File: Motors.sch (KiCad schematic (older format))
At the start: 0 parts

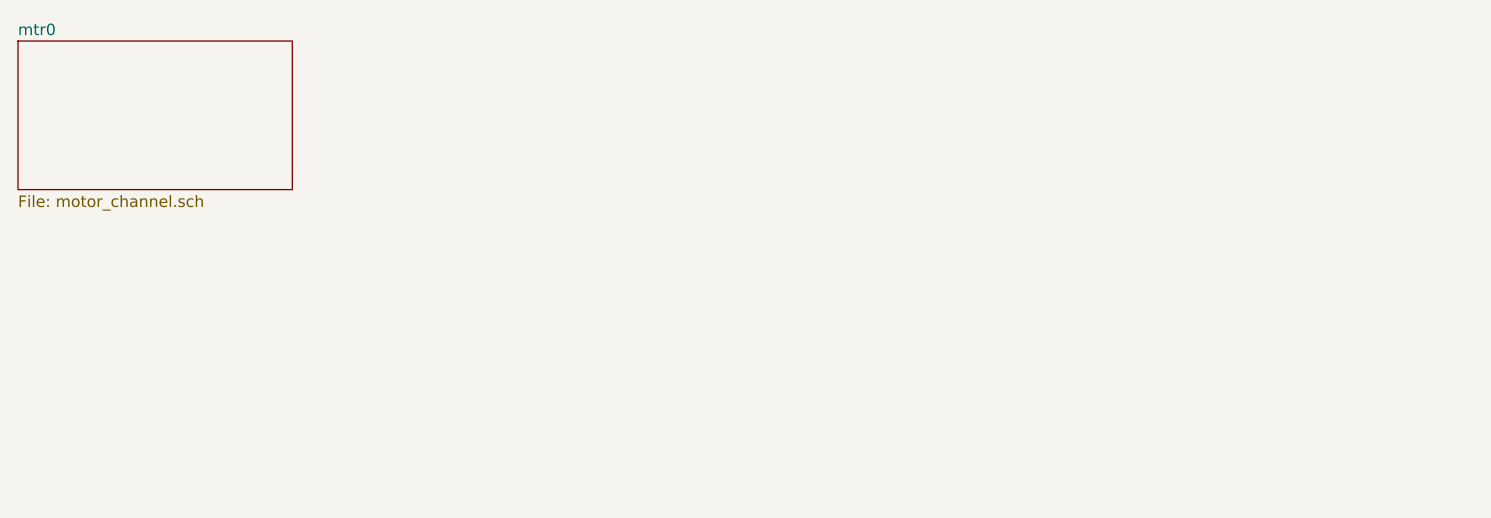
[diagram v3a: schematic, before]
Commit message: Motor channels mostly finished
Todo: Need to determine capacitance of decoupling caps in motor channel.
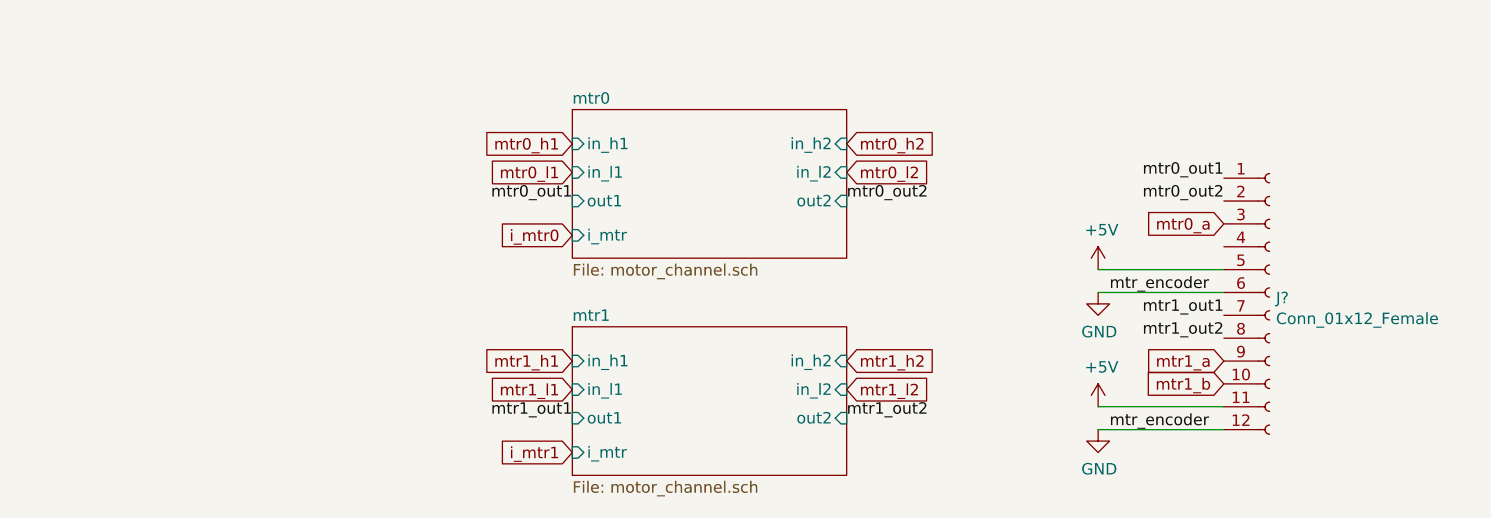
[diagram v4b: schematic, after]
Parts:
- added J?: Conn_01x12_Female, symbol Connector:Conn_01x12_Female
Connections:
- new net +5V: J?.11 (Pin_11), J?.5 (Pin_5)
- new net GND: J?.12 (Pin_12), J?.6 (Pin_6)
- new net mtr0_a: J?.3 (Pin_3)
- new net mtr0_out1: J?.1 (Pin_1)
- new net mtr0_out2: J?.2 (Pin_2)
- new net mtr1_a: J?.9 (Pin_9)
- new net mtr1_b: J?.10 (Pin_10)
- new net mtr1_out1: J?.7 (Pin_7)
- new net mtr1_out2: J?.8 (Pin_8)
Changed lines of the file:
@@
 $Descr A4 11693 8268
 encoding utf-8
-Sheet 10 11
+Sheet 9 12
 Title ""
 Date ""
@@
 $EndDescr
 $Sheet
-S 1100 1050 1200 650
+S 3525 1350 1200 650
 U 5E507A5C
 F0 "mtr0" 50
 F1 "motor_channel.sch" 50
+F2 "in_h1" I L 3525 1500 50
+F3 "in_h2" I R 4725 1500 50
+F4 "in_l1" I L 3525 1625 50
+F5 "in_l2" I R 4725 1625 50
+F6 "i_mtr" I L 3525 1900 50
+F7 "out1" I L 3525 1750 50
+F8 "out2" I R 4725 1750 50
 $EndSheet
+Text Label 3525 1750 2    50   ~ 0
+mtr0_out1
+Text Label 4725 1750 0    50   ~ 0
+mtr0_out2
+Text GLabel 3525 1500 0    50   Input ~ 0
+mtr0_h1
+Text GLabel 3525 1625 0    50   Input ~ 0
+mtr0_l1
+Text GLabel 4725 1500 2    50   Input ~ 0
+mtr0_h2
+Text GLabel 4725 1625 2    50   Input ~ 0
+mtr0_l2
+Text GLabel 3525 1900 0    50   Input ~ 0
+i_mtr0
+$Sheet
+S 3525 2300 1200 650
+U 5E6AD26A
+F0 "mtr1" 50
+F1 "motor_channel.sch" 50
+F2 "in_h1" I L 3525 2450 50
+F3 "in_h2" I R 4725 2450 50
+F4 "in_l1" I L 3525 2575 50
+F5 "in_l2" I R 4725 2575 50
+F6 "i_mtr" I L 3525 2850 50
+F7 "out1" I L 3525 2700 50
+F8 "out2" I R 4725 2700 50
+$EndSheet
+Text Label 3525 2700 2    50   ~ 0
+mtr1_out1
+Text Label 4725 2700 0    50   ~ 0
+mtr1_out2
+Text GLabel 3525 2450 0    50   Input ~ 0
+mtr1_h1
+Text GLabel 3525 2575 0    50   Input ~ 0
+mtr1_l1
+Text GLabel 4725 2450 2    50   Input ~ 0
+mtr1_h2
+Text GLabel 4725 2575 2    50   Input ~ 0
+mtr1_l2
+Text GLabel 3525 2850 0    50   Input ~ 0
+i_mtr1
+$Comp
+L Connector:Conn_01x12_Female J?
+U 1 1 5E6AD3E3
+P 6575 2150
+F 0 "J?" H 6603 2126 50  0000 L CNN
+F 1 "Conn_01x12_Female" H 6603 2035 50  0000 L CNN
+F 2 "" H 6575 2150 50  0001 C CNN
+F 3 "~" H 6575 2150 50  0001 C CNN
+	1    6575 2150
+	1    0    0    -1
+$EndComp
+Text Label 6375 1650 2    50   ~ 0
+mtr0_out1
+Text Label 6375 1750 2    50   ~ 0
+mtr0_out2
+Text GLabel 6375 1850 0    50   Input ~ 0
+mtr0_a
+Text Label 6375 2250 2    50   ~ 0
+mtr1_out1
+Text Label 6375 2350 2    50   ~ 0
+mtr1_out2
+Text GLabel 6375 2450 0    50   Input ~ 0
+mtr1_a
+Text GLabel 6375 2550 0    50   Input ~ 0
+mtr1_b
+Wire Wire Line
+	5825 2050 6375 2050
+Wire Wire Line
+	5825 2150 6375 2150
+Wire Wire Line
+	5825 2650 6375 2650
+Wire Wire Line
+	5825 2750 6375 2750
+$Comp
+L power:+5V #PWR?
+U 1 1 5E6B0E85
+P 5825 2050
+F 0 "#PWR?" H 5825 1900 50  0001 C CNN
+F 1 "+5V" H 5840 2223 50  0000 C CNN
+F 2 "" H 5825 2050 50  0001 C CNN
+F 3 "" H 5825 2050 50  0001 C CNN
+	1    5825 2050
+	1    0    0    -1
+$EndComp
+$Comp
+L power:+5V #PWR?
+U 1 1 5E6B1311
+P 5825 2650
+F 0 "#PWR?" H 5825 2500 50  0001 C CNN
+F 1 "+5V" H 5840 2823 50  0000 C CNN
+F 2 "" H 5825 2650 50  0001 C CNN
+F 3 "" H 5825 2650 50  0001 C CNN
+	1    5825 2650
+	1    0    0    -1
+$EndComp
+$Comp
+L power:GND #PWR?
+U 1 1 5E6B1444
+P 5825 2150
+F 0 "#PWR?" H 5825 1900 50  0001 C CNN
+F 1 "GND" H 5830 1977 50  0000 C CNN
+F 2 "" H 5825 2150 50  0001 C CNN
+F 3 "" H 5825 2150 50  0001 C CNN
+	1    5825 2150
+	1    0    0    -1
+$EndComp
+$Comp
+L power:GND #PWR?
+U 1 1 5E6B180E
+P 5825 2750
+F 0 "#PWR?" H 5825 2500 50  0001 C CNN
+F 1 "GND" H 5830 2577 50  0000 C CNN
+F 2 "" H 5825 2750 50  0001 C CNN
+F 3 "" H 5825 2750 50  0001 C CNN
+	1    5825 2750
+	1    0    0    -1
+$EndComp
+Text Label 5875 2750 0    50   ~ 0
+mtr_encoder
+Text Label 5875 2150 0    50   ~ 0
+mtr_encoder
 $EndSCHEMATC

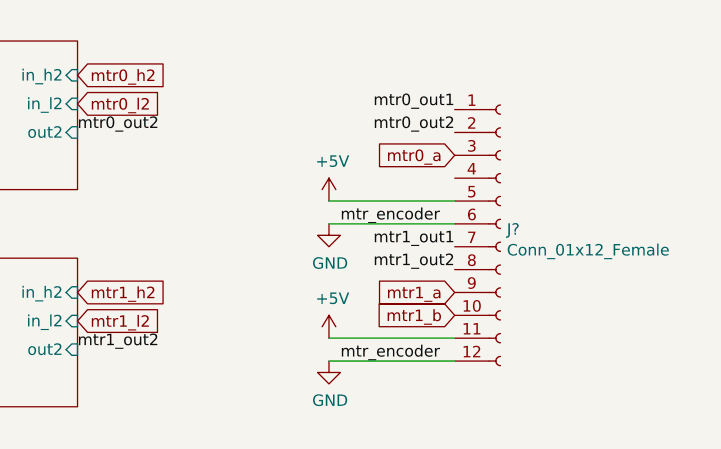
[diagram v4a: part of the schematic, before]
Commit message: hotfix
fixed some labels
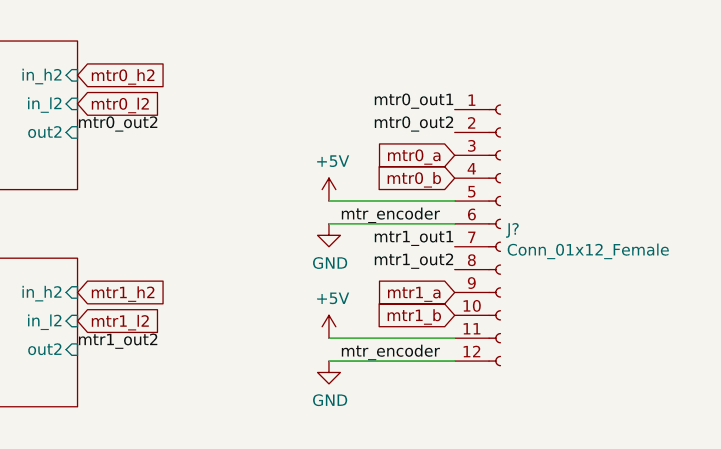
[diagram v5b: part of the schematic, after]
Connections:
- net mtr0_b: now reaches J?.4 (Pin_4)
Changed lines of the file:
@@
 $Descr A4 11693 8268
 encoding utf-8
-Sheet 9 12
+Sheet 10 12
 Title ""
 Date ""
@@
 Text Label 5875 2150 0    50   ~ 0
 mtr_encoder
+Text GLabel 6375 1950 0    50   Input ~ 0
+mtr0_b
 $EndSCHEMATC

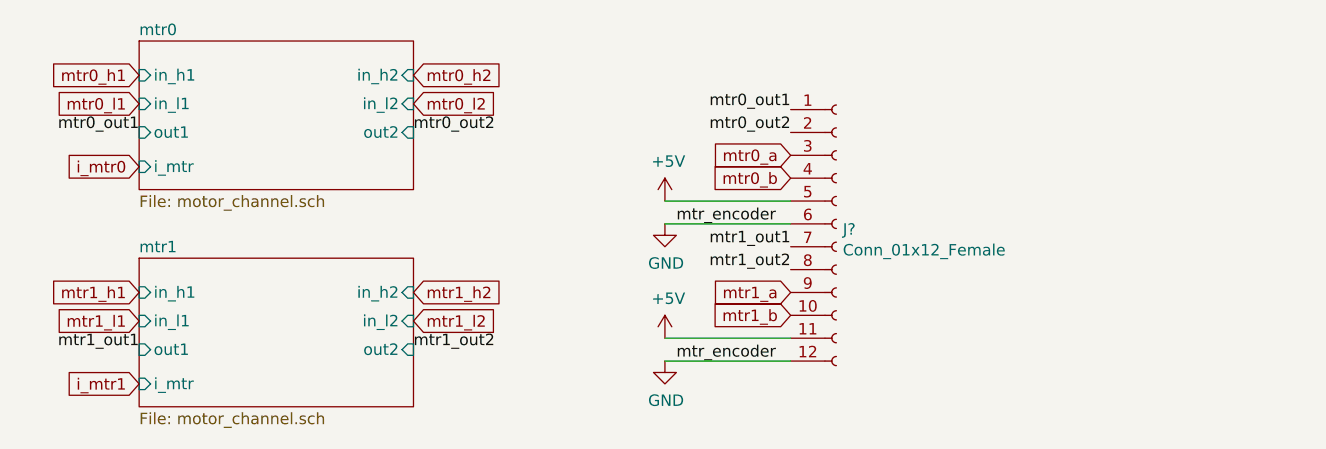
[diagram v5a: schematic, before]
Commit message: Updated Motor Channels
Each motor only needs two inputs.
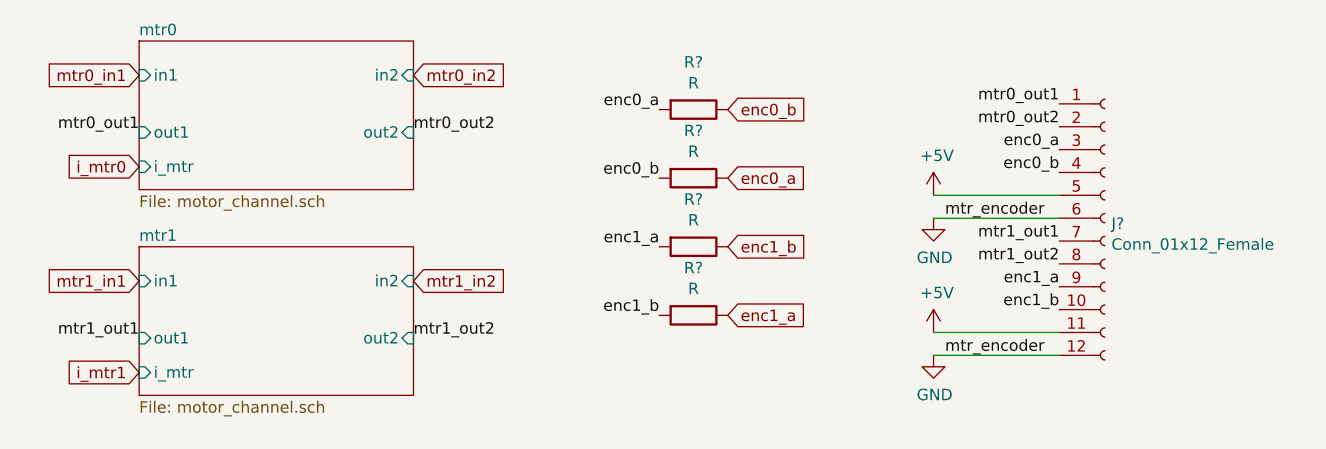
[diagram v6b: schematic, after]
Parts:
- added R? (x4): R, symbol Device:R
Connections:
- net mtr0_a renamed enc0_a
- net enc0_a: now also R?.1, R?.2
- net mtr0_b renamed enc0_b
- net enc0_b: now also R?.1, R?.2
- net mtr1_a renamed enc1_a
- net enc1_a: now also R?.1, R?.2
- net mtr1_b renamed enc1_b
- net enc1_b: now also R?.1, R?.2
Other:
- moved on the sheet: J?
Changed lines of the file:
@@
 F0 "mtr0" 50
 F1 "motor_channel.sch" 50
-F2 "in_h1" I L 3525 1500 50
-F3 "in_h2" I R 4725 1500 50
-F4 "in_l1" I L 3525 1625 50
-F5 "in_l2" I R 4725 1625 50
-F6 "i_mtr" I L 3525 1900 50
-F7 "out1" I L 3525 1750 50
-F8 "out2" I R 4725 1750 50
+F2 "in1" I L 3525 1500 50
+F3 "in2" I R 4725 1500 50
+F4 "i_mtr" I L 3525 1900 50
+F5 "out1" I L 3525 1750 50
+F6 "out2" I R 4725 1750 50
 $EndSheet
 Text Label 3525 1750 2    50   ~ 0
@@
 mtr0_out2
 Text GLabel 3525 1500 0    50   Input ~ 0
-mtr0_h1
-Text GLabel 3525 1625 0    50   Input ~ 0
-mtr0_l1
+mtr0_in1
 Text GLabel 4725 1500 2    50   Input ~ 0
-mtr0_h2
-Text GLabel 4725 1625 2    50   Input ~ 0
-mtr0_l2
+mtr0_in2
 Text GLabel 3525 1900 0    50   Input ~ 0
 i_mtr0
-$Sheet
-S 3525 2300 1200 650
-U 5E6AD26A
-F0 "mtr1" 50
-F1 "motor_channel.sch" 50
-F2 "in_h1" I L 3525 2450 50
-F3 "in_h2" I R 4725 2450 50
-F4 "in_l1" I L 3525 2575 50
-F5 "in_l2" I R 4725 2575 50
-F6 "i_mtr" I L 3525 2850 50
-F7 "out1" I L 3525 2700 50
-F8 "out2" I R 4725 2700 50
-$EndSheet
-Text Label 3525 2700 2    50   ~ 0
-mtr1_out1
-Text Label 4725 2700 0    50   ~ 0
-mtr1_out2
-Text GLabel 3525 2450 0    50   Input ~ 0
-mtr1_h1
-Text GLabel 3525 2575 0    50   Input ~ 0
-mtr1_l1
-Text GLabel 4725 2450 2    50   Input ~ 0
-mtr1_h2
-Text GLabel 4725 2575 2    50   Input ~ 0
-mtr1_l2
-Text GLabel 3525 2850 0    50   Input ~ 0
-i_mtr1
 $Comp
 L Connector:Conn_01x12_Female J?
 U 1 1 5E6AD3E3
-P 6575 2150
-F 0 "J?" H 6603 2126 50  0000 L CNN
-F 1 "Conn_01x12_Female" H 6603 2035 50  0000 L CNN
-F 2 "" H 6575 2150 50  0001 C CNN
-F 3 "~" H 6575 2150 50  0001 C CNN
-	1    6575 2150
+P 7750 2125
+F 0 "J?" H 7778 2101 50  0000 L CNN
+F 1 "Conn_01x12_Female" H 7778 2010 50  0000 L CNN
+F 2 "" H 7750 2125 50  0001 C CNN
+F 3 "~" H 7750 2125 50  0001 C CNN
+	1    7750 2125
 	1    0    0    -1
 $EndComp
-Text Label 6375 1650 2    50   ~ 0
+Text Label 7550 1625 2    50   ~ 0
 mtr0_out1
-Text Label 6375 1750 2    50   ~ 0
+Text Label 7550 1725 2    50   ~ 0
 mtr0_out2
-Text GLabel 6375 1850 0    50   Input ~ 0
-mtr0_a
-Text Label 6375 2250 2    50   ~ 0
+Text GLabel 6100 1950 2    50   Input ~ 0
+enc0_a
+Text Label 7550 2225 2    50   ~ 0
 mtr1_out1
-Text Label 6375 2350 2    50   ~ 0
+Text Label 7550 2325 2    50   ~ 0
 mtr1_out2
-Text GLabel 6375 2450 0    50   Input ~ 0
-mtr1_a
-Text GLabel 6375 2550 0    50   Input ~ 0
-mtr1_b
+Text GLabel 6100 2550 2    50   Input ~ 0
+enc1_a
+Text GLabel 6100 2250 2    50   Input ~ 0
+enc1_b
 Wire Wire Line
-	5825 2050 6375 2050
+	7000 2025 7550 2025
 Wire Wire Line
-	5825 2150 6375 2150
+	7000 2125 7550 2125
 Wire Wire Line
-	5825 2650 6375 2650
+	7000 2625 7550 2625
 Wire Wire Line
-	5825 2750 6375 2750
+	7000 2725 7550 2725
 $Comp
 L power:+5V #PWR?
 U 1 1 5E6B0E85
-P 5825 2050
-F 0 "#PWR?" H 5825 1900 50  0001 C CNN
-F 1 "+5V" H 5840 2223 50  0000 C CNN
-F 2 "" H 5825 2050 50  0001 C CNN
-F 3 "" H 5825 2050 50  0001 C CNN
-	1    5825 2050
+P 7000 2025
+F 0 "#PWR?" H 7000 1875 50  0001 C CNN
+F 1 "+5V" H 7015 2198 50  0000 C CNN
+F 2 "" H 7000 2025 50  0001 C CNN
+F 3 "" H 7000 2025 50  0001 C CNN
+	1    7000 2025
 	1    0    0    -1
 $EndComp
@@
 L power:+5V #PWR?
 U 1 1 5E6B1311
-P 5825 2650
-F 0 "#PWR?" H 5825 2500 50  0001 C CNN
-F 1 "+5V" H 5840 2823 50  0000 C CNN
-F 2 "" H 5825 2650 50  0001 C CNN
-F 3 "" H 5825 2650 50  0001 C CNN
-	1    5825 2650
+P 7000 2625
+F 0 "#PWR?" H 7000 2475 50  0001 C CNN
+F 1 "+5V" H 7015 2798 50  0000 C CNN
+F 2 "" H 7000 2625 50  0001 C CNN
+F 3 "" H 7000 2625 50  0001 C CNN
+	1    7000 2625
 	1    0    0    -1
 $EndComp
@@
 L power:GND #PWR?
 U 1 1 5E6B1444
-P 5825 2150
-F 0 "#PWR?" H 5825 1900 50  0001 C CNN
-F 1 "GND" H 5830 1977 50  0000 C CNN
-F 2 "" H 5825 2150 50  0001 C CNN
-F 3 "" H 5825 2150 50  0001 C CNN
-	1    5825 2150
+P 7000 2125
+F 0 "#PWR?" H 7000 1875 50  0001 C CNN
+F 1 "GND" H 7005 1952 50  0000 C CNN
+F 2 "" H 7000 2125 50  0001 C CNN
+F 3 "" H 7000 2125 50  0001 C CNN
+	1    7000 2125
 	1    0    0    -1
 $EndComp
@@
 L power:GND #PWR?
 U 1 1 5E6B180E
-P 5825 2750
-F 0 "#PWR?" H 5825 2500 50  0001 C CNN
-F 1 "GND" H 5830 2577 50  0000 C CNN
-F 2 "" H 5825 2750 50  0001 C CNN
-F 3 "" H 5825 2750 50  0001 C CNN
-	1    5825 2750
+P 7000 2725
+F 0 "#PWR?" H 7000 2475 50  0001 C CNN
+F 1 "GND" H 7005 2552 50  0000 C CNN
+F 2 "" H 7000 2725 50  0001 C CNN
+F 3 "" H 7000 2725 50  0001 C CNN
+	1    7000 2725
 	1    0    0    -1
 $EndComp
-Text Label 5875 2750 0    50   ~ 0
+Text Label 7050 2725 0    50   ~ 0
 mtr_encoder
-Text Label 5875 2150 0    50   ~ 0
+Text Label 7050 2125 0    50   ~ 0
 mtr_encoder
-Text GLabel 6375 1950 0    50   Input ~ 0
-mtr0_b
+Text GLabel 6100 1650 2    50   Input ~ 0
+enc0_b
+$Sheet
+S 3525 2250 1200 650
+U 5E6EF1BC
+F0 "mtr1" 50
+F1 "motor_channel.sch" 50
+F2 "in1" I L 3525 2400 50
+F3 "in2" I R 4725 2400 50
+F4 "i_mtr" I L 3525 2800 50
+F5 "out1" I L 3525 2650 50
+F6 "out2" I R 4725 2650 50
+$EndSheet
+Text Label 3525 2650 2    50   ~ 0
+mtr1_out1
+Text Label 4725 2650 0    50   ~ 0
+mtr1_out2
+Text GLabel 3525 2400 0    50   Input ~ 0
+mtr1_in1
+Text GLabel 4725 2400 2    50   Input ~ 0
+mtr1_in2
+Text GLabel 3525 2800 0    50   Input ~ 0
+i_mtr1
+$Comp
+L Device:R R?
+U 1 1 5E6FBB13
+P 5950 1650
+F 0 "R?" V 5743 1650 50  0000 C CNN
+F 1 "R" V 5834 1650 50  0000 C CNN
+F 2 "" V 5880 1650 50  0001 C CNN
+F 3 "~" H 5950 1650 50  0001 C CNN
+	1    5950 1650
+	0    1    1    0
+$EndComp
+Text Label 7550 1825 2    50   ~ 0
+enc0_a
+Text Label 7550 1925 2    50   ~ 0
+enc0_b
+Text Label 7550 2425 2    50   ~ 0
+enc1_a
+Text Label 7550 2525 2    50   ~ 0
+enc1_b
+Text Label 5800 1650 2    50   ~ 0
+enc0_a
+Text Label 5800 1950 2    50   ~ 0
+enc0_b
+$Comp
+L Device:R R?
+U 1 1 5E700368
+P 5950 1950
+F 0 "R?" V 5743 1950 50  0000 C CNN
+F 1 "R" V 5834 1950 50  0000 C CNN
+F 2 "" V 5880 1950 50  0001 C CNN
+F 3 "~" H 5950 1950 50  0001 C CNN
+	1    5950 1950
+	0    1    1    0
+$EndComp
+$Comp
+L Device:R R?
+U 1 1 5E701D8F
+P 5950 2250
+F 0 "R?" V 5743 2250 50  0000 C CNN
+F 1 "R" V 5834 2250 50  0000 C CNN
+F 2 "" V 5880 2250 50  0001 C CNN
+F 3 "~" H 5950 2250 50  0001 C CNN
+	1    5950 2250
+	0    1    1    0
+$EndComp
+$Comp
+L Device:R R?
+U 1 1 5E7027C7
+P 5950 2550
+F 0 "R?" V 5743 2550 50  0000 C CNN
+F 1 "R" V 5834 2550 50  0000 C CNN
+F 2 "" V 5880 2550 50  0001 C CNN
+F 3 "~" H 5950 2550 50  0001 C CNN
+	1    5950 2550
+	0    1    1    0
+$EndComp
+Text Label 5800 2250 2    50   ~ 0
+enc1_a
+Text Label 5800 2550 2    50   ~ 0
+enc1_b
 $EndSCHEMATC
